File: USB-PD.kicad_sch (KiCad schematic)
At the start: 59 parts, among them IC3 TPS7A0518PDBVT, J1 1053131102, J12 E8124-015-01, Q10 Si7223DN, Q11 Si7223DN, Q12 BSS84AKW, Q14 BSS84AKW, Q9 SQS401EN-T1_BE3, U12 STUSB4500QTR, U14 LTC4418IUF#PBF

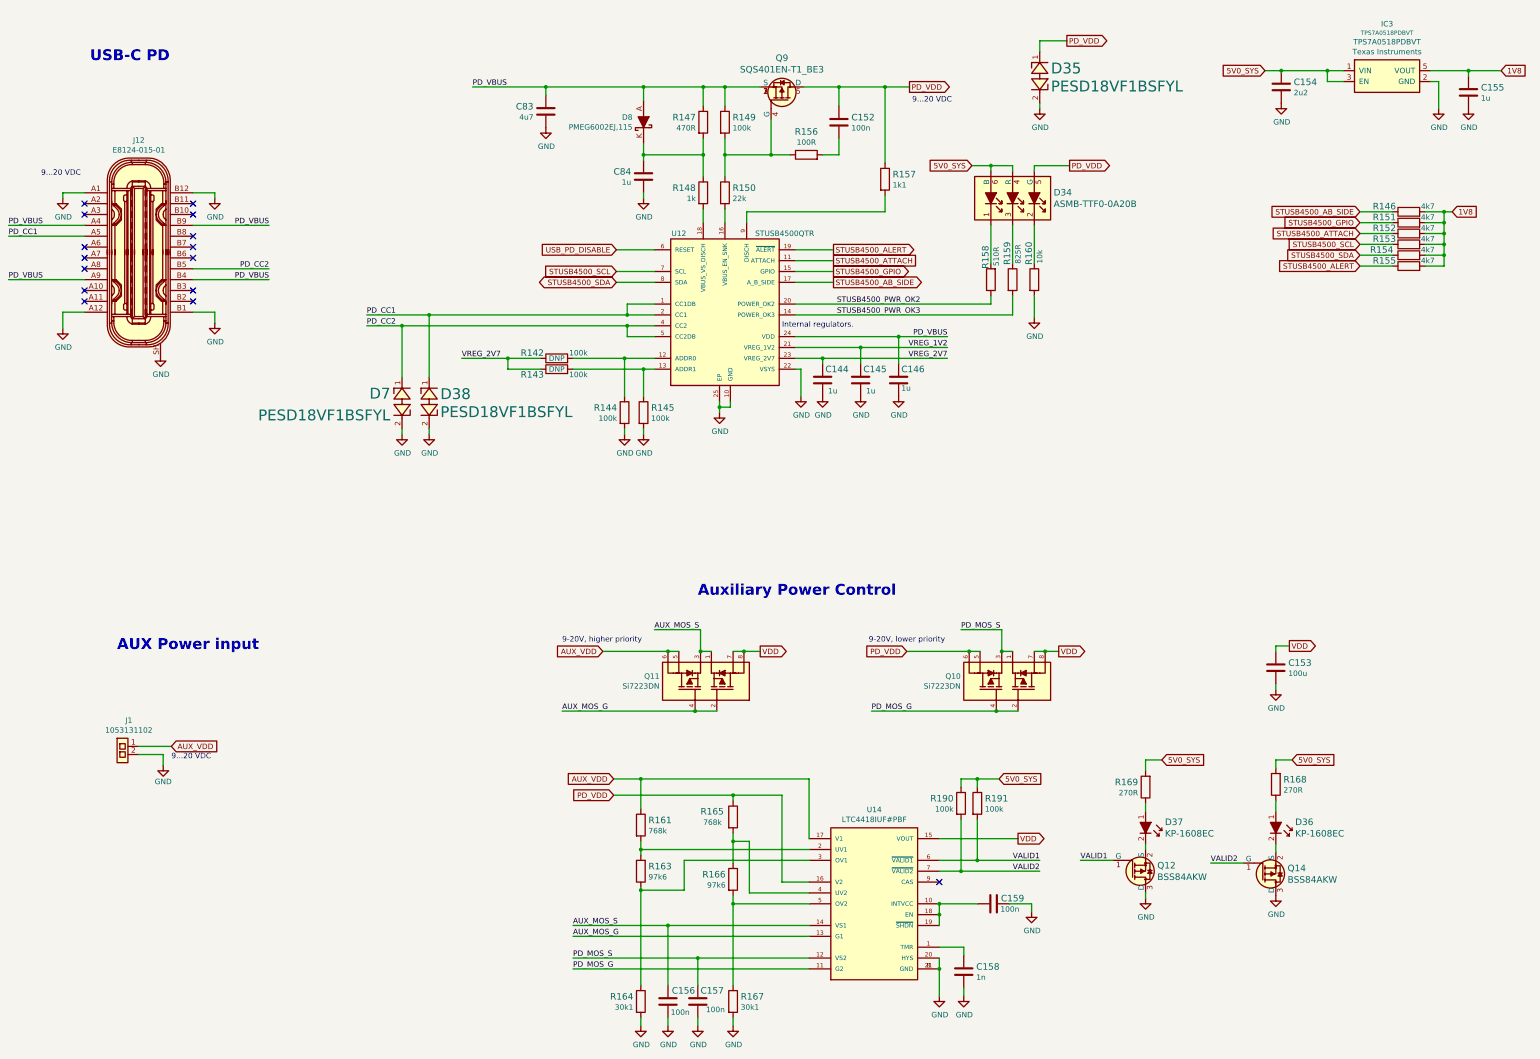
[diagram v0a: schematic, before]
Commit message: Introduce component standardization
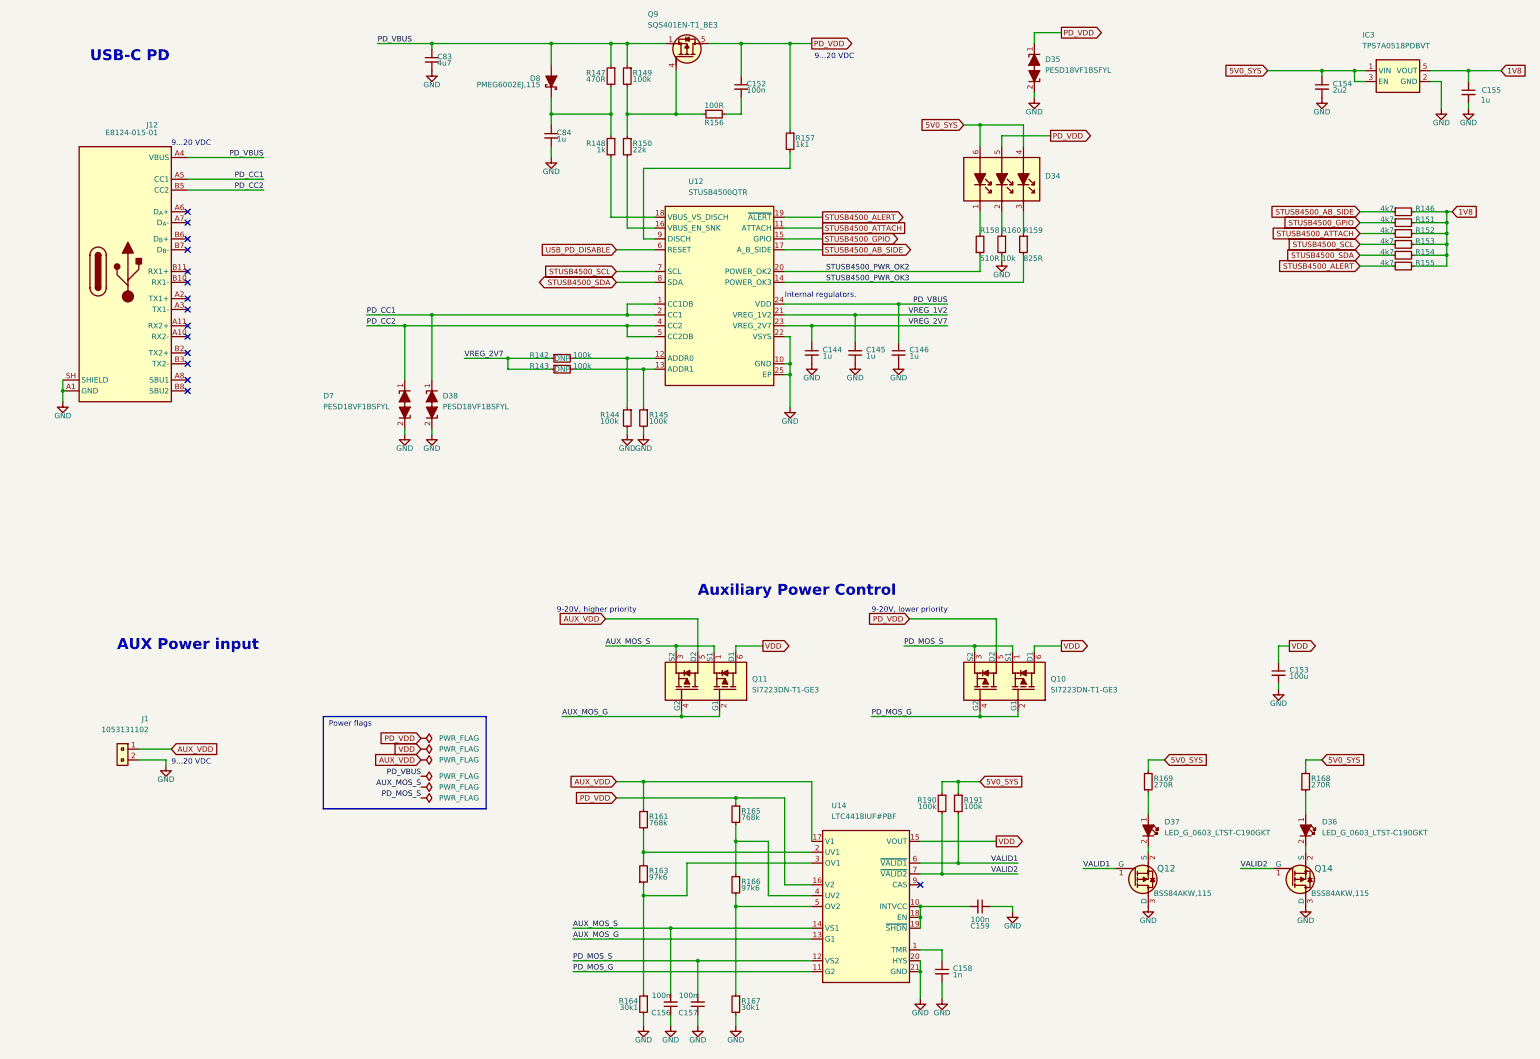
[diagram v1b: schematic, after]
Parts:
- C144, C145, C146, C154, C155: footprint sc606-baseboard-footprints:0402-cap -> sc606-baseboard-footprints:C_0402_1005Metric; Author (none) -> Antmicro; License (none) -> Apache-2.0
- C152, C156, C157, C159: footprint sc606-baseboard-footprints:0402-cap -> sc606-baseboard-footprints:C_0402_1005Metric; Author (none) -> Antmicro; Dielectric (none) -> X5R; License (none) -> Apache-2.0; Voltage (none) -> 50V
- C153: footprint sc606-baseboard-footprints:0805-cap -> sc606-baseboard-footprints:C_0805_2012Metric; Author (none) -> Antmicro; License (none) -> Apache-2.0; Manufacturer MURATA -> Murata
- C158: footprint sc606-baseboard-footprints:0402-res -> sc606-baseboard-footprints:C_0402_1005Metric; Author (none) -> Antmicro; Dielectric (none) -> C0G; License (none) -> Apache-2.0; MPN CC0402KRX7R9BB102 -> GRM1555C1H102JA01D; Manufacturer YAGEO -> Murata; Voltage (none) -> 50V
- C83: footprint sc606-baseboard-footprints:0603-cap -> sc606-baseboard-footprints:C_0603_1608Metric; Author (none) -> Antmicro; License (none) -> Apache-2.0
- C84: footprint sc606-baseboard-footprints:0603-cap -> sc606-baseboard-footprints:C_0603_1608Metric; Author (none) -> Antmicro; License (none) -> Apache-2.0; Manufacturer WALSIN -> Walsin
- D34, Q12, Q14, Q9: Author (none) -> Antmicro; License (none) -> Apache-2.0
- D35, D38, D7: footprint sc606-baseboard-footprints:RESC0603X26N -> sc606-baseboard-footprints:D_0201_0603Metric; Author (none) -> Antmicro; License (none) -> Apache-2.0; Manufacturer nexperia -> Nexperia
- D36, D37: value KP-1608EC -> LED_G_0603_LTST-C190GKT; footprint sc606-baseboard-footprints:LED_0603 -> sc606-baseboard-footprints:LED_0603_1608Metric_G; symbol sc606-baseboard:KP-1608EC -> sc606-baseboard:LED_G_0603_LTST-C190GKT; Author (none) -> Antmicro; License (none) -> Apache-2.0; MPN KP-1608EC -> LTST-C190GKT; Manufacturer KINGBRIGHT -> Lite-On Inc.
- D8: footprint sc606-baseboard-footprints:SOD-323F -> sc606-baseboard-footprints:D_SOD-323F; Author (none) -> Antmicro; License (none) -> Apache-2.0; Manufacturer NEXPERIA -> Nexperia
- IC3: value TPS7A0518PDBVT -> TPS7A0518P_SOT23-5; symbol sc606-baseboard:TPS7A0518PDBVT -> sc606-baseboard:TPS7A0518P_SOT23-5; Author (none) -> Antmicro; License (none) -> Apache-2.0
- J1: value 1053131102 -> PinHeader_1x2_P2.5mm_Drill1.1mm_Shrouded_Latch; footprint sc606-baseboard-footprints:1053131102 -> sc606-baseboard-footprints:PinHeader_1x2_P2.5mm_Drill1.1mm_Shrouded_Latch; symbol sc606-baseboard:1053131102 -> sc606-baseboard:PinHeader_1x2_P2.5mm_Drill1.1mm_Shrouded_Latch; Author (none) -> Antmicro; License (none) -> Apache-2.0
- J12: value E8124-015-01 -> E8124-015-01_separate; symbol sc606-baseboard:E8124-015-01 -> sc606-baseboard:E8124-015-01_separate; Author (none) -> Antmicro; License (none) -> Apache-2.0; Manufacturer Pulse Electronics Network -> Pulse
- Q10, Q11: footprint sc606-baseboard-footprints:PowerPak-1212 -> sc606-baseboard-footprints:Vishay_PowerPAK_1212-8_Dual; Author (none) -> Antmicro; License (none) -> Apache-2.0; Manufacturer VISHAY -> Vishay
- R142, R143, R144, R145, R149, R190, R191: footprint sc606-baseboard-footprints:0402-res -> sc606-baseboard-footprints:R_0402_1005Metric; Author (none) -> Antmicro; License (none) -> Apache-2.0; MPN CRCW0402100KFKEDHP -> CR0402-FX-1003GLF; Manufacturer VISHAY -> Bourns; Tolerance (none) -> 1%
- R146, R151, R152, R153, R154, R155: footprint sc606-baseboard-footprints:0402-res -> sc606-baseboard-footprints:R_0402_1005Metric; Author (none) -> Antmicro; License (none) -> Apache-2.0; MPN MCS04020C4701FE000 -> CR0402-FX-4701GLF; Manufacturer VISHAY -> Bourns; Tolerance (none) -> 1%
- R147: footprint sc606-baseboard-footprints:0402-res -> sc606-baseboard-footprints:R_0402_1005Metric; Author (none) -> Antmicro; License (none) -> Apache-2.0; MPN CRCW0402470RFKED -> CR0402-FX-4700GLF; Manufacturer VISHAY -> Bourns; Tolerance (none) -> 1%
- R148, R156: footprint sc606-baseboard-footprints:0402-res -> sc606-baseboard-footprints:R_0402_1005Metric; Author (none) -> Antmicro; License (none) -> Apache-2.0; Manufacturer BOURNS -> Bourns; Tolerance (none) -> 1%
- R150: footprint sc606-baseboard-footprints:0402-res -> sc606-baseboard-footprints:R_0402_1005Metric; Author (none) -> Antmicro; License (none) -> Apache-2.0; MPN ERJ-2RKF2202X -> CR0402-FX-2202GLF; Manufacturer Panasonic -> Bourns; Tolerance (none) -> 1%
- R157: footprint sc606-baseboard-footprints:0402-res -> sc606-baseboard-footprints:R_0402_1005Metric; Author (none) -> Antmicro; License (none) -> Apache-2.0; MPN ERJ2RKF1101X -> CR0402-FX-1101GLF; Manufacturer PANASONIC_ELECTRONIC_COMPONENTS -> Bourns; Tolerance (none) -> 1%
- R158: footprint sc606-baseboard-footprints:0402-res -> sc606-baseboard-footprints:R_0402_1005Metric; Author (none) -> Antmicro; License (none) -> Apache-2.0; MPN RC0402JR-07510RL -> CR0402-FX-5100GLF; Manufacturer Yageo -> Bourns; Tolerance (none) -> 1%
- R159: footprint sc606-baseboard-footprints:0402-res -> sc606-baseboard-footprints:R_0402_1005Metric; Author (none) -> Antmicro; License (none) -> Apache-2.0; MPN ERJ2RKF8250X -> CR0402-FX-8250GLF; Manufacturer PANASONIC -> Bourns; Tolerance (none) -> 1%
- R160: footprint sc606-baseboard-footprints:0402-res -> sc606-baseboard-footprints:R_0402_1005Metric; Author (none) -> Antmicro; License (none) -> Apache-2.0; MPN CRCW040210K0FKEDHP -> CR0402-FX-1002GLF; Manufacturer VISHAY -> Bourns; Tolerance (none) -> 1%
- R161, R165: footprint sc606-baseboard-footprints:0402-res -> sc606-baseboard-footprints:R_0402_1005Metric; Author (none) -> Antmicro; License (none) -> Apache-2.0; MPN CRCW0402768KFKED -> CR0402-FX-7683GLF; Manufacturer Vishay -> Bourns; Tolerance (none) -> 1%
- R163, R166: footprint sc606-baseboard-footprints:0402-res -> sc606-baseboard-footprints:R_0402_1005Metric; Author (none) -> Antmicro; License (none) -> Apache-2.0; MPN MCMR04X9762FTL -> CR0402-FX-9762GLF; Manufacturer MULTICOMP -> Bourns; Tolerance (none) -> 1%
- R164, R167: footprint sc606-baseboard-footprints:0603-res -> sc606-baseboard-footprints:R_0603_1608Metric; Author (none) -> Antmicro; License (none) -> Apache-2.0; MPN CRCW060330K1FKEA -> CR0603-FX-3012ELF; Manufacturer VISHAY -> Bourns; Tolerance (none) -> 1%
- R168, R169: footprint sc606-baseboard-footprints:0603-res -> sc606-baseboard-footprints:R_0603_1608Metric; Author (none) -> Antmicro; License (none) -> Apache-2.0; MPN ERJ3EKF2700V -> CR0603-FX-2700ELF; Manufacturer Panasonic -> Bourns; Tolerance (none) -> 1%
- U12: value STUSB4500QTR -> STUSB4500_QFN; footprint sc606-baseboard-footprints:QFN50P400X400X90-25N -> sc606-baseboard-footprints:QFN-24-1EP_4x4mm_EP2.1x2.1mm; symbol sc606-baseboard:STUSB4500QTR -> sc606-baseboard:STUSB4500_QFN; Author (none) -> Antmicro; License (none) -> Apache-2.0
- U14: value LTC4418IUF#PBF -> LTC4418; footprint sc606-baseboard-footprints:QFN-20_1EP_4x4_P0.5mm -> sc606-baseboard-footprints:QFN-20-1EP_4x4mm_P0.5mm_EP2.45x2.45mm; symbol sc606-baseboard:LTC4418IUF#PBF -> sc606-baseboard:LTC4418; Author (none) -> Antmicro; License (none) -> Apache-2.0; MANUFACTURER AnalogDevices -> (none); Manufacturer (none) -> Analog Devices
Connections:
- net AUX_VDD: no longer Q11.6
- net PD_VDD: no longer Q10.6
- net VDD: now also Q10.6 (D1), Q11.6 (D1); no longer Q10.7, Q10.8, Q11.7, Q11.8
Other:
- note added: "Power flags"
- moved on the sheet: C144, C145, C146, C152, C153, C154, C155, C156, C157, C158, C159, C83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

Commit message: [#61796] Run globlib
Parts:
- C144, C145, C146, C155: footprint sc606-baseboard-footprints:C_0402_1005Metric -> antmicro-footprints:C_0402_1005Metric; symbol sc606-baseboard:C_1u_0402 -> antmicroCapacitors0402:C_1u_0402
- C152, C156, C157, C159: footprint sc606-baseboard-footprints:C_0402_1005Metric -> antmicro-footprints:C_0402_1005Metric; symbol sc606-baseboard:C_100n_0402 -> antmicroCapacitors0402:C_100n_0402
- C153: footprint sc606-baseboard-footprints:C_0805_2012Metric -> antmicro-footprints:C_0805_2012Metric; symbol sc606-baseboard:C_100u_0805 -> antmicroCapacitorsmisc:C_100u_0805
- C154: footprint sc606-baseboard-footprints:C_0402_1005Metric -> antmicro-footprints:C_0402_1005Metric; symbol sc606-baseboard:C_2u2_0402 -> antmicroCapacitors0402:C_2u2_0402
- C158: footprint sc606-baseboard-footprints:C_0402_1005Metric -> antmicro-footprints:C_0402_1005Metric; symbol sc606-baseboard:C_1n_0402 -> antmicroCapacitors0402:C_1n_0402
- C83: footprint sc606-baseboard-footprints:C_0603_1608Metric -> antmicro-footprints:C_0603_1608Metric; symbol sc606-baseboard:C_4u7_0603 -> antmicroCapacitors0603:C_4u7_0603
- C84: footprint sc606-baseboard-footprints:C_0603_1608Metric -> antmicro-footprints:C_0603_1608Metric; symbol sc606-baseboard:C_1u_0603 -> antmicroCapacitors0603:C_1u_0603
- D34: footprint sc606-baseboard-footprints:PLCC6_3.5x3.7mm -> antmicro-footprints:PLCC6_3.5x3.7mm; symbol sc606-baseboard:ASMB-TTF0-0A20B -> antmicroLEDIndicationDiscrete:LED_RGB_PLCC6_ASMB-TTF0-0A20B
- D35, D38, D7: footprint sc606-baseboard-footprints:D_0201_0603Metric -> antmicro-footprints:D_0201_0603Metric; symbol sc606-baseboard:PESD18VF1BSFYL -> antmicroTVSDiodes:PESD18VF1BSFYL
- D36, D37: footprint sc606-baseboard-footprints:LED_0603_1608Metric_G -> antmicro-footprints:LED_0603_1608Metric_G; symbol sc606-baseboard:LED_G_0603_LTST-C190GKT -> antmicroLEDIndicationDiscrete:LED_G_0603_LTST-C190GKT
- D8: footprint sc606-baseboard-footprints:D_SOD-323F -> antmicro-footprints:D_SOD-323F; symbol sc606-baseboard:PMEG6002EJ,115 -> antmicroDiodesRectifiersSingle:PMEG6002EJ,115
- IC3: footprint sc606-baseboard-footprints:SOT-23-5 -> antmicro-footprints:SOT-23-5; symbol sc606-baseboard:TPS7A0518P_SOT23-5 -> antmicroPMICVoltageRegulatorsLinear:TPS7A0518P_SOT23-5
- J1: footprint sc606-baseboard-footprints:PinHeader_1x2_P2.5mm_Drill1.1mm_Shrouded_Latch -> antmicro-footprints:Conn_Molex_Nano-Fit_1x2_1053131102; symbol sc606-baseboard:PinHeader_1x2_P2.5mm_Drill1.1mm_Shrouded_Latch -> antmicroWire2BoardConnectors:Molex_Nano-Fit_1x2_1053131102
- J12: footprint sc606-baseboard-footprints:USB-C_Female_E8124-015-01 -> antmicro-footprints:USB-C_Receptacle_PulseElectronics_E8124-015-01; symbol sc606-baseboard:E8124-015-01_separate -> antmicroUSBConnectors:USB-C_PulseElectronics_E8124-015-01
- Q10, Q11: footprint sc606-baseboard-footprints:Vishay_PowerPAK_1212-8_Dual -> antmicro-footprints:Vishay_PowerPAK_1212-8_Dual; symbol sc606-baseboard:Si7223DN -> antmicroTransistorsFETsMOSFETsArrays:Si7223DN
- Q12, Q14: footprint sc606-baseboard-footprints:SOT-323 -> antmicro-footprints:SOT-323; symbol sc606-baseboard:BSS84AKW -> antmicroTransistorsFETsMOSFETsSingle:BSS84AKW
- Q9: footprint sc606-baseboard-footprints:Vishay_PowerPAK_1212-8_Single -> antmicro-footprints:Vishay_PowerPAK_1212-8_Single; symbol sc606-baseboard:SQS401EN-T1_BE3 -> antmicroTransistorsFETsMOSFETsSingle:SQS401EN-T1_BE3
- R142, R143, R144, R145, R149, R190, R191: footprint sc606-baseboard-footprints:R_0402_1005Metric -> antmicro-footprints:R_0402_1005Metric; symbol sc606-baseboard:R_100k_0402 -> antmicroResistors0402:R_100k_0402
- R146, R151, R152, R153, R154, R155: footprint sc606-baseboard-footprints:R_0402_1005Metric -> antmicro-footprints:R_0402_1005Metric; symbol sc606-baseboard:R_4k7_0402 -> antmicroResistors0402:R_4k7_0402
- R147: footprint sc606-baseboard-footprints:R_0402_1005Metric -> antmicro-footprints:R_0402_1005Metric; symbol sc606-baseboard:R_470R_0402 -> antmicroResistors0402:R_470R_0402
- R148: footprint sc606-baseboard-footprints:R_0402_1005Metric -> antmicro-footprints:R_0402_1005Metric; symbol sc606-baseboard:R_1k_0402 -> antmicroResistors0402:R_1k_0402
- R150: footprint sc606-baseboard-footprints:R_0402_1005Metric -> antmicro-footprints:R_0402_1005Metric; symbol sc606-baseboard:R_22k_0402 -> antmicroResistors0402:R_22k_0402
- R156: footprint sc606-baseboard-footprints:R_0402_1005Metric -> antmicro-footprints:R_0402_1005Metric; symbol sc606-baseboard:R_100R_0402 -> antmicroResistors0402:R_100R_0402
- R157: footprint sc606-baseboard-footprints:R_0402_1005Metric -> antmicro-footprints:R_0402_1005Metric; symbol sc606-baseboard:R_1k1_0402 -> antmicroResistors0402:R_1k1_0402
- R158: footprint sc606-baseboard-footprints:R_0402_1005Metric -> antmicro-footprints:R_0402_1005Metric; symbol sc606-baseboard:R_510R_0402 -> antmicroResistors0402:R_510R_0402
- R159: footprint sc606-baseboard-footprints:R_0402_1005Metric -> antmicro-footprints:R_0402_1005Metric; symbol sc606-baseboard:R_825R_0402 -> antmicroResistors0402:R_825R_0402
- R160: footprint sc606-baseboard-footprints:R_0402_1005Metric -> antmicro-footprints:R_0402_1005Metric; symbol sc606-baseboard:R_10k_0402 -> antmicroResistors0402:R_10k_0402
- R161, R165: footprint sc606-baseboard-footprints:R_0402_1005Metric -> antmicro-footprints:R_0402_1005Metric; symbol sc606-baseboard:R_768k_0402 -> antmicroResistors0402:R_768k_0402
- R163, R166: footprint sc606-baseboard-footprints:R_0402_1005Metric -> antmicro-footprints:R_0402_1005Metric; symbol sc606-baseboard:R_97k6_0402 -> antmicroResistors0402:R_97k6_0402
- R164, R167: footprint sc606-baseboard-footprints:R_0603_1608Metric -> antmicro-footprints:R_0603_1608Metric; symbol sc606-baseboard:R_30k1_0603 -> antmicroResistors0603:R_30k1_0603
- R168, R169: footprint sc606-baseboard-footprints:R_0603_1608Metric -> antmicro-footprints:R_0603_1608Metric; symbol sc606-baseboard:R_270R_0603 -> antmicroResistors0603:R_270R_0603
- U12: footprint sc606-baseboard-footprints:QFN-24-1EP_4x4mm_EP2.1x2.1mm -> antmicro-footprints:QFN-24-1EP_4x4mm_P0.5_EP2.1x2.1mm; symbol sc606-baseboard:STUSB4500_QFN -> antmicroPMICPowerDistributionSwitchesLoadDrivers:STUSB4500_QFN
- U14: footprint sc606-baseboard-footprints:QFN-20-1EP_4x4mm_P0.5mm_EP2.45x2.45mm -> antmicro-footprints:QFN-20-1EP_4x4mm_P0.5mm_EP2.45x2.45mm; symbol sc606-baseboard:LTC4418 -> antmicroPMICPowerDistributionSwitchesLoadDrivers:LTC4418

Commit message: [#61796] Update schematics
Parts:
- C84: Manufacturer Walsin -> KYOCERA AVX
- D34: value ASMB-TTF0-0A20B -> LED_RGB_PLCC6_ASMB-TTF0-0A20B; Color (none) -> R, G, B
- D36, D37: Color (none) -> Green; Manufacturer Lite-On Inc. -> Lite-On
- J1: value PinHeader_1x2_P2.5mm_Drill1.1mm_Shrouded_Latch -> Molex_Nano-Fit_1x2_1053131102
- J12: value E8124-015-01_separate -> USB-C_PulseElectronics_E8124-015-01; Manufacturer Pulse -> Pulse Electronics
- R142, R143: now not fitted; now left out of the parts list
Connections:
- net 5V0_SYS: now also D34.1 (A_{R}), D34.5 (A_{B}); no longer D34.4, D34.6
- net PD_VBUS: now also D8.2 (A); no longer D8.A
- net PD_VDD: now also D34.3 (A_{G}); no longer D34.5
- net VBUS_EN_SNK: now reaches R150.2, U12.16 (VBUS_EN_SNK)
- net VBUS_VS_DISCH: now reaches R148.2, U12.18 (VBUS_VS_DISCH)
- net DISCH: now reaches R157.2, U12.9 (DISCH)
- net at C84.1, R147.2, R148.1: now also D8.1 (C); no longer D8.K
- net at R168.1: now also D36.2 (A); no longer D36.1
- net at R169.1: now also D37.2 (A); no longer D37.1
- net at R158.2: now also D34.6 (C_{B}); no longer D34.1
- net at D34.2 (C_{R}): now also R159.1; no longer R160.1
- net at Q14.2 (S): now also D36.1 (C); no longer D36.2
- net at Q12.2 (S): now also D37.1 (C); no longer D37.2
- new net: D34.4 (C_{G}), R160.1
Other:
- note added: "Internal regulators"
- note removed: "Internal regulators."
- company: (none) -> Antmicro Ltd
- moved on the sheet: C144, C145, C146, C154, C156, C157, C158, C159, D36, D37, J12, R157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
